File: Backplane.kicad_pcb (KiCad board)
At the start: 2 copper layers, 92.2 x 91.7 mm, 11 parts, among them J1 Ext Power in, J2 Int/Ext power select, U1 Edge_connector_Male, U2 Edge_connector_Male, U3 Edge_connector_Male, U4 Edge_connector_Male, U5 Edge_connector_Male

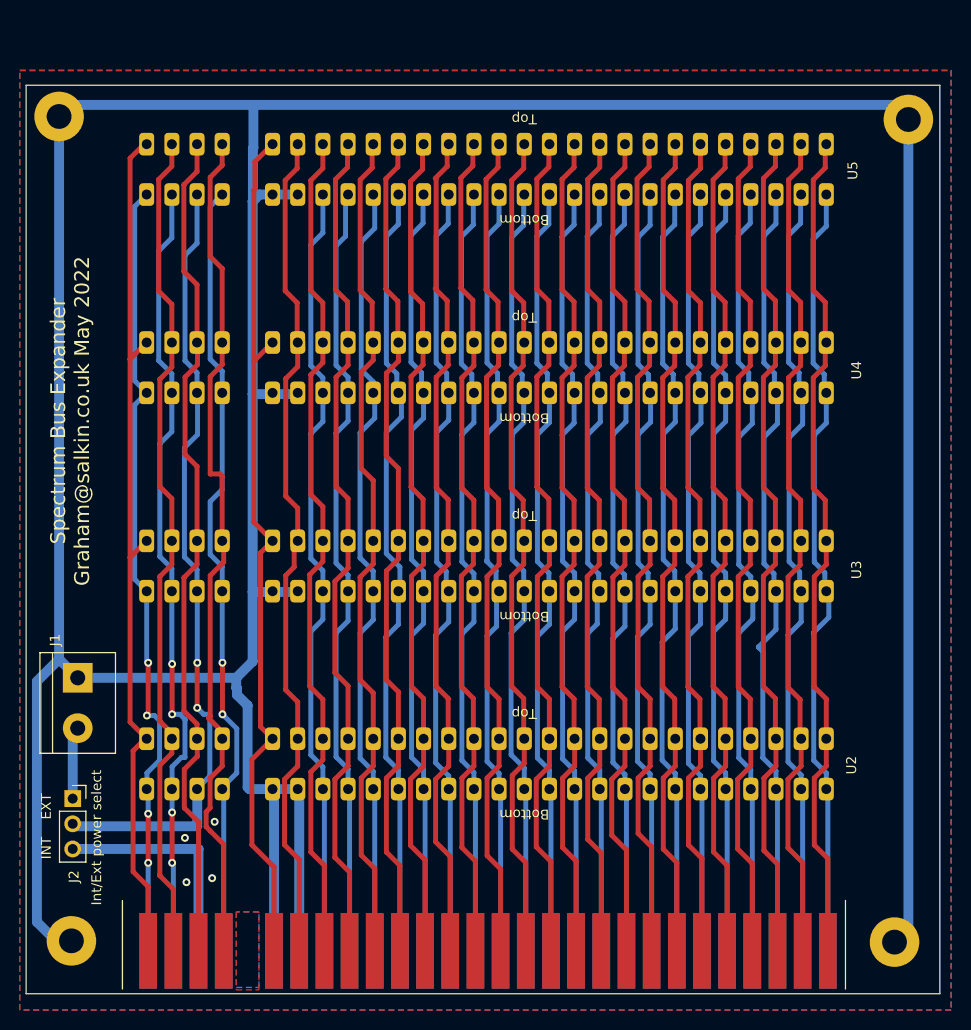
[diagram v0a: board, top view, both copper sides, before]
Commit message: Added updated PCB and images. Corrected the fact the sockets were reversed
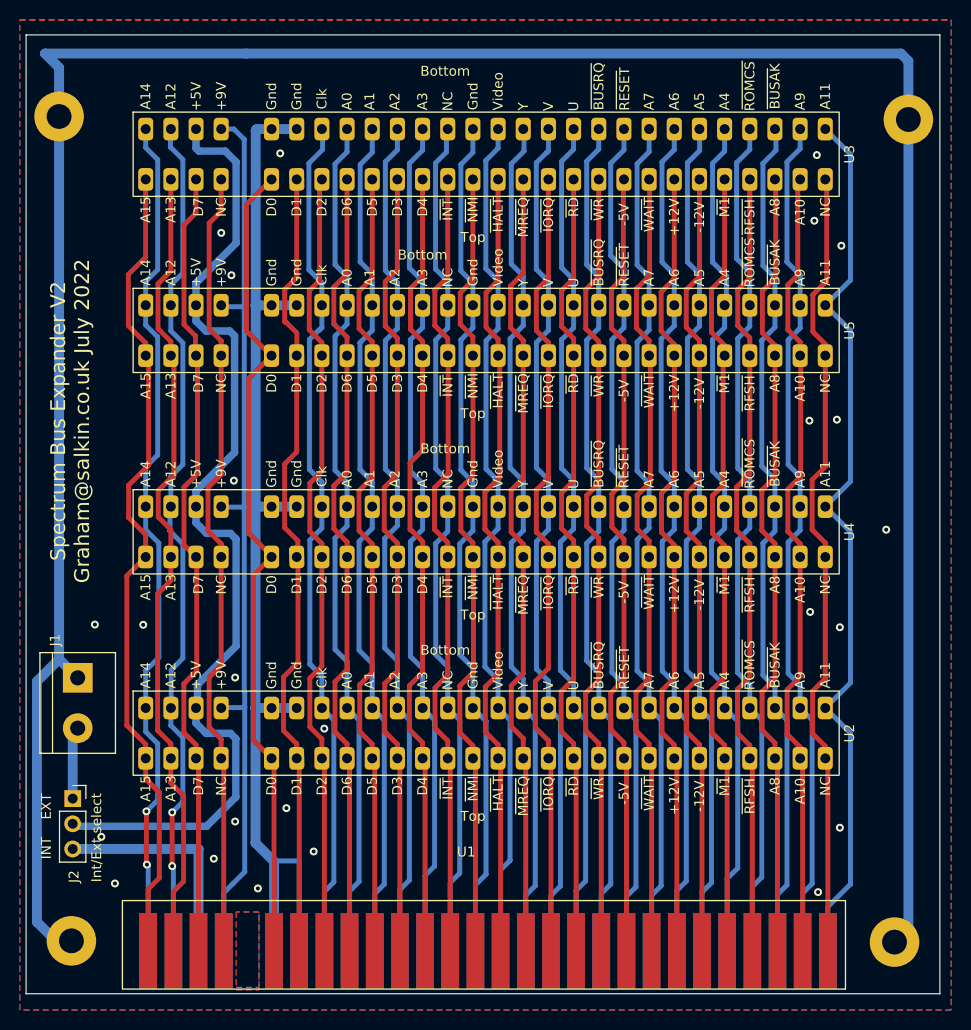
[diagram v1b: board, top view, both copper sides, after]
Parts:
- J2: value Int/Ext power select -> Int/Ext select
- U1: footprint SpeccyEdge:Speccy_edge -> Spectrum:Speccy_edge_External
- U2, U3, U4, U5: footprint SpeccyEdge:Speccy_edge_Socket -> Spectrum:Speccy_edge_Socket_reversed
- moved U3 41.9 mm to (185.4, 66.0), turned to 0 degrees
- moved U4 17.4 mm to (185.4, 104.1), turned to 0 degrees
- moved U5 17.1 mm to (185.4, 83.8), turned to 0 degrees
- moved U2 6.04 mm to (185.4, 124.5), turned to 0 degrees
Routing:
- net /+5V: track 79.4 -> 102.5 mm, vias 2 -> 0
- net /+9V: track 79.6 -> 92.7 mm, vias 2 -> 0
- net GND: track 399.5 -> 386.6 mm, vias 4 -> 25
- net /A11: track 79.2 -> 91.2 mm
- net /Video: track 78.8 -> 87.0 mm
- net /A9: track 78.9 -> 86.9 mm
- net /U: track 78.9 -> 87.0 mm
- net /A5: track 78.9 -> 87.0 mm
- net /A4: track 79.0 -> 87.0 mm
- net //BUSRQ: track 79.0 -> 86.9 mm
- net /0V1: track 79.1 -> 87.0 mm
- net /V: track 79.0 -> 86.9 mm
- net /A3: track 79.1 -> 86.9 mm
- net /A6: track 79.1 -> 86.9 mm
- net (no net): track 79.4 -> 87.2 mm
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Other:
- board size 92.2 x 91.7 mm -> 92.2 x 96.7 mm
- board text added: "Spectrum Bus Expander V2 Graham@salkin.co.uk July 2022"
- board text removed: "Spectrum Bus Expander Graham@salkin.co.uk May 2022"
